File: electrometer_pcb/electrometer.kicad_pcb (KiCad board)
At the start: 2 copper layers, 50 x 50 mm, 27 parts, among them J2 Conn_01x03_Pin, J3 Screw_Terminal_01x03, J4 PRT-14417, U1 LMC6082, U2 ADS1115IDGS, U3 REF3025, U4 5V LDO, U5 INA159AIDGKR

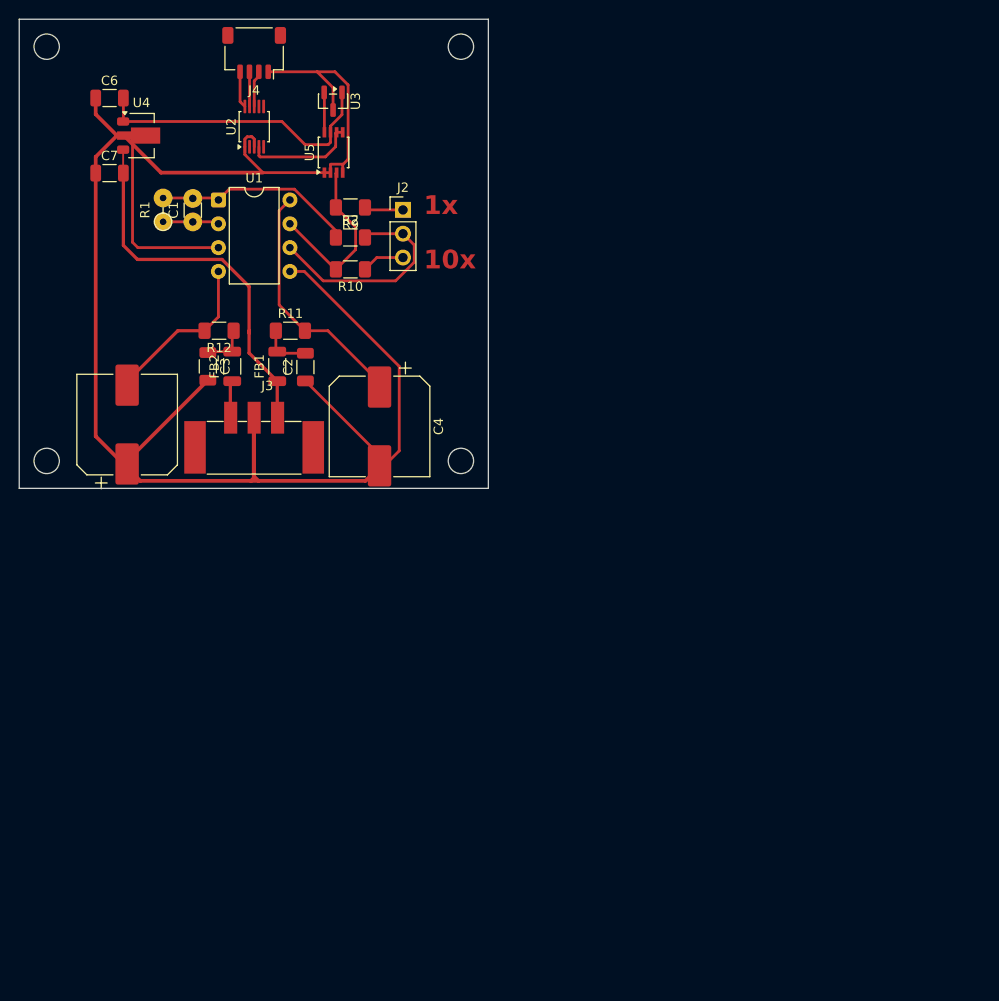
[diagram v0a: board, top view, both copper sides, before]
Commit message: added board for inductor probe/gitignore to ignore those pesky history folders
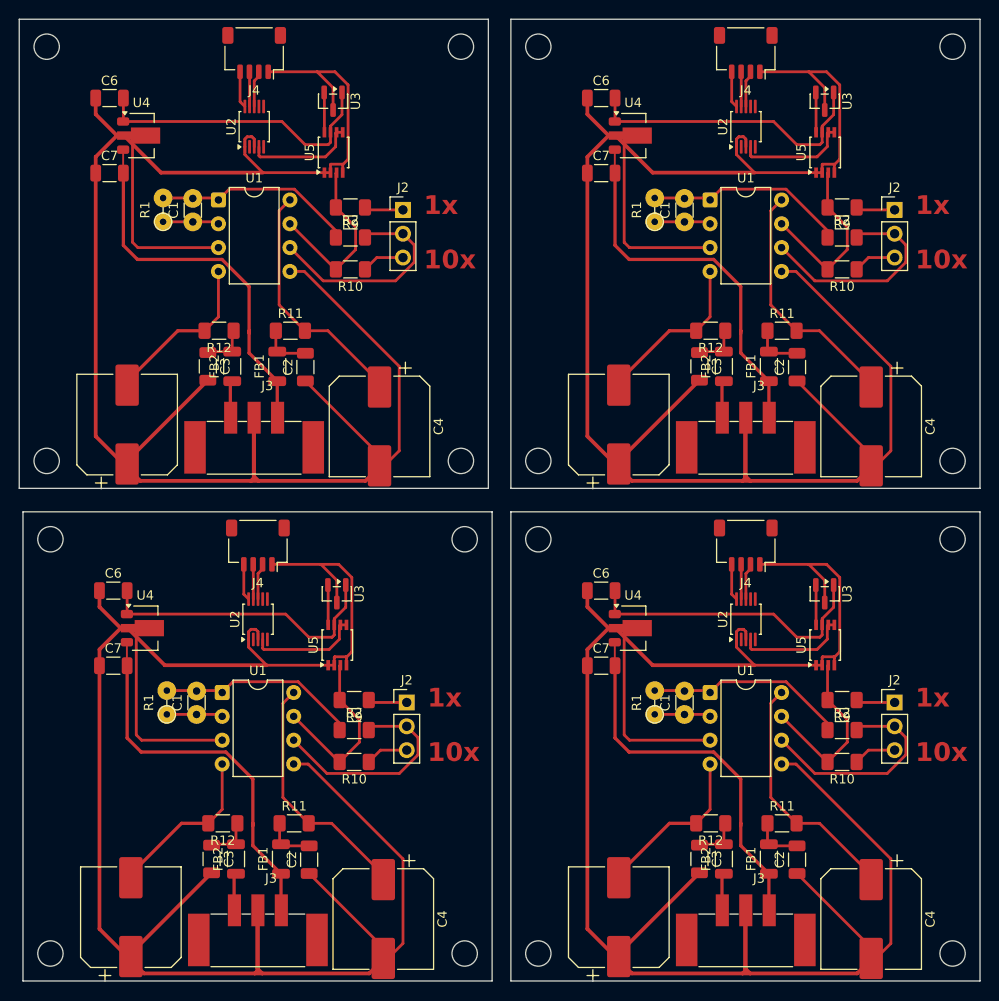
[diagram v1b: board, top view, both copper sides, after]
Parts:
- added C1: 100p, Capacitor_THT:C_Disc_D3.0mm_W1.6mm_P2.50mm, F.Cu at (147.0, 116.6)
- added C1: 100p, Capacitor_THT:C_Disc_D3.0mm_W1.6mm_P2.50mm, F.Cu at (95.0, 169.1)
- added C1: 100p, Capacitor_THT:C_Disc_D3.0mm_W1.6mm_P2.50mm, F.Cu at (147.0, 169.1)
- added C2: 100n, Capacitor_SMD:C_1206_3216Metric, F.Cu at (159.0, 132.1)
- added C2: 100n, Capacitor_SMD:C_1206_3216Metric, F.Cu at (159.0, 184.6)
- added C2: 100n, Capacitor_SMD:C_1206_3216Metric, F.Cu at (107.0, 184.6)
- added C3: 100n, Capacitor_SMD:C_1206_3216Metric, F.Cu at (96.6, 184.5)
- added C3: 100n, Capacitor_SMD:C_1206_3216Metric, F.Cu at (148.6, 184.5)
- added C3: 100n, Capacitor_SMD:C_1206_3216Metric, F.Cu at (148.6, 132.0)
- added C4: C_Polarized, Capacitor_SMD:CP_Elec_10x10.5, F.Cu at (166.9, 138.4)
- added C4: C_Polarized, Capacitor_SMD:CP_Elec_10x10.5, F.Cu at (114.9, 190.9)
- added C4: C_Polarized, Capacitor_SMD:CP_Elec_10x10.5, F.Cu at (166.9, 190.9)
- added C5: C_Polarized, Capacitor_SMD:CP_Elec_10x10.5, F.Cu at (140.0, 138.2)
- added C5: C_Polarized, Capacitor_SMD:CP_Elec_10x10.5, F.Cu at (140.0, 190.7)
- added C5: C_Polarized, Capacitor_SMD:CP_Elec_10x10.5, F.Cu at (88.0, 190.7)
- added C6: 100n, Capacitor_SMD:C_1206_3216Metric, F.Cu at (86.1, 155.9)
- added C6: 100n, Capacitor_SMD:C_1206_3216Metric, F.Cu at (138.1, 103.4)
- added C6: 100n, Capacitor_SMD:C_1206_3216Metric, F.Cu at (138.1, 155.9)
- added C7: 100n, Capacitor_SMD:C_1206_3216Metric, F.Cu at (138.1, 163.9)
- added C7: 100n, Capacitor_SMD:C_1206_3216Metric, F.Cu at (138.1, 111.4)
- added C7: 100n, Capacitor_SMD:C_1206_3216Metric, F.Cu at (86.1, 163.9)
- added FB1: FerriteBead, Inductor_SMD:L_1206_3216Metric, F.Cu at (104.0, 184.5)
- added FB1: FerriteBead, Inductor_SMD:L_1206_3216Metric, F.Cu at (156.0, 132.0)
- added FB1: FerriteBead, Inductor_SMD:L_1206_3216Metric, F.Cu at (156.0, 184.5)
- added FB2: FerriteBead, Inductor_SMD:L_1206_3216Metric, F.Cu at (151.2, 184.5)
- added FB2: FerriteBead, Inductor_SMD:L_1206_3216Metric, F.Cu at (99.2, 184.5)
- added FB2: FerriteBead, Inductor_SMD:L_1206_3216Metric, F.Cu at (151.2, 132.0)
- added J2: Conn_01x03_Pin, Connector_PinHeader_2.54mm:PinHeader_1x03_P2.54mm_Vertical, F.Cu at (169.4, 115.3)
- added J2: Conn_01x03_Pin, Connector_PinHeader_2.54mm:PinHeader_1x03_P2.54mm_Vertical, F.Cu at (117.4, 167.8)
- added J2: Conn_01x03_Pin, Connector_PinHeader_2.54mm:PinHeader_1x03_P2.54mm_Vertical, F.Cu at (169.4, 167.8)
- added J3: Screw_Terminal_01x03, TerminalBlock_Phoenix:TerminalBlock_Phoenix_PTSM-0,5-3-2,5-V-SMD_1x03-1MP_P2.50mm_Vertical, F.Cu at (101.5, 192.1)
- added J3: Screw_Terminal_01x03, TerminalBlock_Phoenix:TerminalBlock_Phoenix_PTSM-0,5-3-2,5-V-SMD_1x03-1MP_P2.50mm_Vertical, F.Cu at (153.5, 192.1)
- added J3: Screw_Terminal_01x03, TerminalBlock_Phoenix:TerminalBlock_Phoenix_PTSM-0,5-3-2,5-V-SMD_1x03-1MP_P2.50mm_Vertical, F.Cu at (153.5, 139.6)
- added J4: PRT-14417, Connector_JST:JST_SH_SM04B-SRSS-TB_1x04-1MP_P1.00mm_Horizontal, F.Cu at (153.5, 98.6)
- added J4: PRT-14417, Connector_JST:JST_SH_SM04B-SRSS-TB_1x04-1MP_P1.00mm_Horizontal, F.Cu at (101.5, 151.1)
- added J4: PRT-14417, Connector_JST:JST_SH_SM04B-SRSS-TB_1x04-1MP_P1.00mm_Horizontal, F.Cu at (153.5, 151.1)
- added R1: 5G, Resistor_THT:R_Axial_DIN0204_L3.6mm_D1.6mm_P2.54mm_Vertical, F.Cu at (91.8, 169.1)
- added R1: 5G, Resistor_THT:R_Axial_DIN0204_L3.6mm_D1.6mm_P2.54mm_Vertical, F.Cu at (143.8, 169.1)
- added R1: 5G, Resistor_THT:R_Axial_DIN0204_L3.6mm_D1.6mm_P2.54mm_Vertical, F.Cu at (143.8, 116.6)
- added R10: 10k, Resistor_SMD:R_1206_3216Metric_Pad1.30x1.75mm_HandSolder, F.Cu at (163.8, 121.7)
- added R10: 10k, Resistor_SMD:R_1206_3216Metric_Pad1.30x1.75mm_HandSolder, F.Cu at (111.8, 174.2)
- added R10: 10k, Resistor_SMD:R_1206_3216Metric_Pad1.30x1.75mm_HandSolder, F.Cu at (163.8, 174.2)
- added R11: 10, Resistor_SMD:R_1206_3216Metric_Pad1.30x1.75mm_HandSolder, F.Cu at (157.4, 180.7)
- added R11: 10, Resistor_SMD:R_1206_3216Metric_Pad1.30x1.75mm_HandSolder, F.Cu at (157.4, 128.2)
- added R11: 10, Resistor_SMD:R_1206_3216Metric_Pad1.30x1.75mm_HandSolder, F.Cu at (105.4, 180.7)
- added R12: 10, Resistor_SMD:R_1206_3216Metric_Pad1.30x1.75mm_HandSolder, F.Cu at (149.8, 128.2)
- added R12: 10, Resistor_SMD:R_1206_3216Metric_Pad1.30x1.75mm_HandSolder, F.Cu at (97.8, 180.7)
- added R12: 10, Resistor_SMD:R_1206_3216Metric_Pad1.30x1.75mm_HandSolder, F.Cu at (149.8, 180.7)
- added R2: 1k, Resistor_SMD:R_1206_3216Metric_Pad1.30x1.75mm_HandSolder, F.Cu at (163.8, 118.3)
- added R2: 1k, Resistor_SMD:R_1206_3216Metric_Pad1.30x1.75mm_HandSolder, F.Cu at (163.8, 170.8)
- added R2: 1k, Resistor_SMD:R_1206_3216Metric_Pad1.30x1.75mm_HandSolder, F.Cu at (111.8, 170.8)
- added R9: 1k, Resistor_SMD:R_1206_3216Metric_Pad1.30x1.75mm_HandSolder, F.Cu at (163.8, 167.6)
- added R9: 1k, Resistor_SMD:R_1206_3216Metric_Pad1.30x1.75mm_HandSolder, F.Cu at (163.8, 115.1)
- added R9: 1k, Resistor_SMD:R_1206_3216Metric_Pad1.30x1.75mm_HandSolder, F.Cu at (111.8, 167.6)
- added REF**: MountingHole_2.7mm, MountingHole:MountingHole_2.7mm, F.Cu at (131.4, 142.1)
- added REF**: MountingHole_2.7mm, MountingHole:MountingHole_2.7mm, F.Cu at (123.6, 194.6)
- added REF**: MountingHole_2.7mm, MountingHole:MountingHole_2.7mm, F.Cu at (79.4, 194.6)
- added REF**: MountingHole_2.7mm, MountingHole:MountingHole_2.7mm, F.Cu at (123.6, 150.4)
- added REF**: MountingHole_2.7mm, MountingHole:MountingHole_2.7mm, F.Cu at (175.6, 142.1)
- added REF**: MountingHole_2.7mm, MountingHole:MountingHole_2.7mm, F.Cu at (131.4, 97.9)
- added REF**: MountingHole_2.7mm, MountingHole:MountingHole_2.7mm, F.Cu at (175.6, 194.6)
- added REF**: MountingHole_2.7mm, MountingHole:MountingHole_2.7mm, F.Cu at (175.6, 97.9)
- added REF**: MountingHole_2.7mm, MountingHole:MountingHole_2.7mm, F.Cu at (79.4, 150.4)
- added REF**: MountingHole_2.7mm, MountingHole:MountingHole_2.7mm, F.Cu at (131.4, 150.4)
- added REF**: MountingHole_2.7mm, MountingHole:MountingHole_2.7mm, F.Cu at (131.4, 194.6)
- added REF**: MountingHole_2.7mm, MountingHole:MountingHole_2.7mm, F.Cu at (175.6, 150.4)
- added U1: LMC6082, Package_DIP:DIP-8_W7.62mm, F.Cu at (149.7, 114.3)
- added U1: LMC6082, Package_DIP:DIP-8_W7.62mm, F.Cu at (97.7, 166.8)
- added U1: LMC6082, Package_DIP:DIP-8_W7.62mm, F.Cu at (149.7, 166.8)
- added U2: ADS1115IDGS, Package_SO:TSSOP-10_3x3mm_P0.5mm, F.Cu at (153.5, 159.0)
- added U2: ADS1115IDGS, Package_SO:TSSOP-10_3x3mm_P0.5mm, F.Cu at (153.5, 106.5)
- added U2: ADS1115IDGS, Package_SO:TSSOP-10_3x3mm_P0.5mm, F.Cu at (101.5, 159.0)
- added U3: REF3025, Package_TO_SOT_SMD:SOT-23, F.Cu at (161.9, 156.2)
- added U3: REF3025, Package_TO_SOT_SMD:SOT-23, F.Cu at (110.0, 156.2)
- added U3: REF3025, Package_TO_SOT_SMD:SOT-23, F.Cu at (161.9, 103.7)
- added U4: 5V LDO, Package_TO_SOT_SMD:SOT-89-3, F.Cu at (89.5, 159.9)
- added U4: 5V LDO, Package_TO_SOT_SMD:SOT-89-3, F.Cu at (141.5, 159.9)
- added U4: 5V LDO, Package_TO_SOT_SMD:SOT-89-3, F.Cu at (141.5, 107.4)
- added U5: INA159AIDGKR, Package_SO:TSSOP-8_3x3mm_P0.65mm, F.Cu at (162.0, 161.7)
- added U5: INA159AIDGKR, Package_SO:TSSOP-8_3x3mm_P0.65mm, F.Cu at (162.0, 109.2)
- added U5: INA159AIDGKR, Package_SO:TSSOP-8_3x3mm_P0.65mm, F.Cu at (110.0, 161.7)
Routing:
- net GND: track 215.6 -> 862.6 mm
- net V+: track 40.9 -> 163.7 mm
- net +5V: track 31.6 -> 126.3 mm
- net Net-(U1C-V+): track 26.3 -> 105.1 mm
- net Net-(J2-Pin_2): track 23.3 -> 93.2 mm
- net Net-(C1-Pad2): track 21.5 -> 86.2 mm
- net /Output: track 19.0 -> 76.0 mm
- net Net-(U1C-V-): track 18.2 -> 72.7 mm
- net Net-(U2-AIN0): track 11.9 -> 47.4 mm
- net Net-(U1A--): track 5.99 -> 23.9 mm
- net Net-(C2-Pad2): track 5.36 -> 21.4 mm
- net Net-(C3-Pad1): track 4.93 -> 19.7 mm
- net Net-(J2-Pin_3): track 4.57 -> 18.3 mm
- net +2V5: track 4.26 -> 17.0 mm
- net Net-(J2-Pin_1): track 4.16 -> 16.6 mm
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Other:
- board size 50 x 50 mm -> 102.4 x 102.5 mm
